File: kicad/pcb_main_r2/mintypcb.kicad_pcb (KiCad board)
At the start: 2 copper layers, 89 x 55.5 mm, 158 parts, among them J101 USB_C_Receptacle_USB2.0_14P, J102 S2B-PH-SM4-TB, J103 FPC09-Q1.0-8, J106 Conn_02x15_Odd_Even, J107 Conn_02x15_Odd_Even, J108 Conn_02x15_Odd_Even, Q101 3415, Q102 3415, Q103 BSS138, SW101 SKQGABE010, SW102 SKRRAAE010, SW103 SKQGABE010, SW104 SKRRAAE010, SW105 SKQGABE010, SW106 SKRRAAE010, SW107 see note 1, SW108 SKRRAAE010, SW109 see note 1, SW110 SKRRAAE010, SW111 see note 1, SW112 SKRRAAE010, SW113 see note 1, SW114 SKRRAAE010, SW115 SKQGABE010, SW116 SKRRAAE010, U101 LMV393, U102 MCP73833T-FCI/MF, U103 PAM2401SCADJ, U104 MAX98357A, U106 74AHCT1G125, U107 USBLC6-2SC6

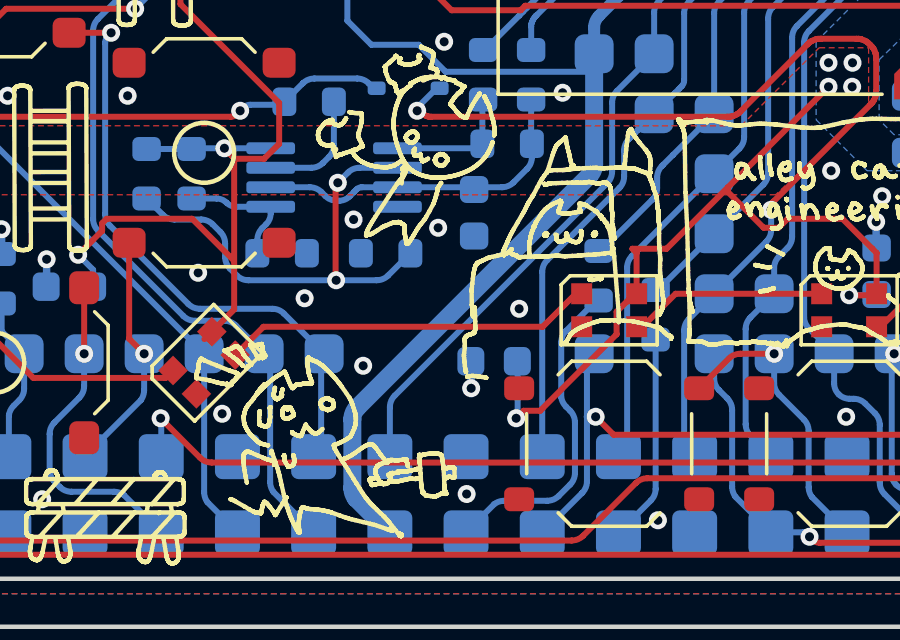
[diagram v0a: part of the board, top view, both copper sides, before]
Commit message: changed display brightness control port
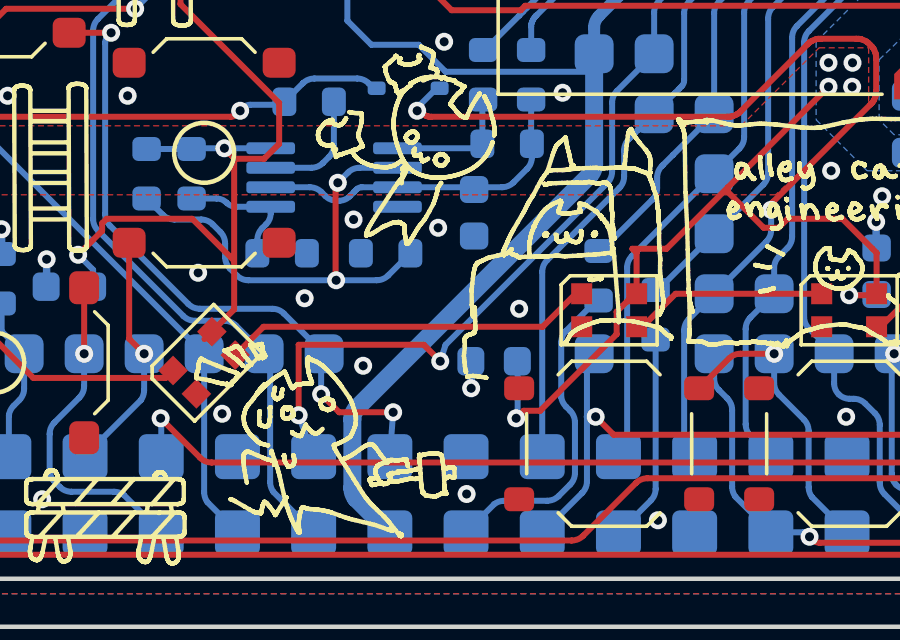
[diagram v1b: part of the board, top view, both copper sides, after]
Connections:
- A101 pad 16: /UP -> /RST
- A101 pad 18: /RST -> /UP
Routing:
- net /RST: track 23.8 -> 28.7 mm, vias 0 -> 2
- net /UP: track 20.6 -> 22.5 mm, vias 1 -> 3
